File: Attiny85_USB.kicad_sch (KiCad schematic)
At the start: 0 parts

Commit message: Add full KiCad project with symbols and backups
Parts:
- added C1: 100n, Capacitor_SMD:C_1206_3216Metric_Pad1.33x1.80mm_HandSolder, symbol Device:C
- added D1, D2: 3V6, Diode_SMD:D_SOD-123, symbol Device:D_Zener
- added D3: LED, symbol Device:LED
- added J1, J2: Conn_01x04, symbol Connector_Generic:Conn_01x04
- added R1, R2: 68R, Resistor_SMD:R_0805_2012Metric_Pad1.20x1.40mm_HandSolder, symbol Device:R
- added R3: 330R, Resistor_SMD:R_0805_2012Metric_Pad1.20x1.40mm_HandSolder, symbol Device:R
- added R4: 1k5, Resistor_SMD:R_0805_2012Metric_Pad1.20x1.40mm_HandSolder, symbol Device:R
- added U1: ATtiny85-20M, Package_DFN_QFN:QFN-20-1EP_4x4mm_P0.5mm_EP2.6x2.6mm, symbol MCU_Microchip_ATtiny:ATtiny85-20M
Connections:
- new net: D2.1 (K), R2.2, R4.2
- new net: D1.1 (K), R1.2
- new net: J1.1 (Pin_1), U1.11 (AREF/PB0)
- new net: J1.2 (Pin_2), R3.1, U1.12 (PB1)
- new net: J1.3 (Pin_3), U1.14 (PB2)
- new net: J2.2 (Pin_2), R2.1, U1.2 (XTAL1/PB3)
- new net: D3.2 (A), R3.2
- new net: J2.3 (Pin_3), R1.1, U1.5 (XTAL2/PB4)
- new net: J2.1 (Pin_1), U1.1 (~{RESET}/PB5)
- new net +5V: C1.1, J1.4 (Pin_4), R4.1, U1.15 (VCC)
- new net GND: C1.2, D1.2 (A), D2.2 (A), D3.1 (K), J2.4 (Pin_4), U1.21 (GND), U1.8 (GND)

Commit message: added my symbol
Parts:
- added U2: ~, symbol my_symbol:PCB_USB_connector
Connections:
- net +5V: now also U2.1 (Vcc)
- net GND: now also U2.4 (GND)
- net at D2.1 (K), R2.2, R4.2: now also U2.2 (D+)
- net at D1.1 (K), R1.2: now also U2.3 (D-)
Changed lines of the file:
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@@
+	)
+	(junction
+		(at 156.21 57.15)
+		(diameter 0)
+		(color 0 0 0 0)
 	)
 	(junction
@@
 	)
 	(junction
+		(at 168.91 96.52)
+		(diameter 0)
+		(color 0 0 0 0)
+	)
+	(junction
 		(at 156.21 63.5)
 		(diameter 0)
@@
 	)
 	(junction
+		(at 156.21 33.02)
+		(diameter 0)
+		(color 0 0 0 0)
+	)
+	(junction
+		(at 168.91 67.31)
+		(diameter 0)
+		(color 0 0 0 0)
+	)
+	(junction
 		(at 119.38 62.23)
 		(diameter 0)
@@
 	(wire
 		(pts
+			(xy 182.88 96.52) (xy 168.91 96.52)
+		)
+		(stroke
+			(width 0)
+			(type default)
+		)
+	)
+	(wire
+		(pts
 			(xy 168.91 96.52) (xy 168.91 91.44)
 		)
@@
 	(wire
 		(pts
+			(xy 170.18 53.34) (xy 170.18 33.02)
+		)
+		(stroke
+			(width 0)
+			(type default)
+		)
+	)
+	(wire
+		(pts
 			(xy 120.65 62.23) (xy 119.38 62.23)
 		)
@@
 	(wire
 		(pts
+			(xy 182.88 60.96) (xy 168.91 60.96)
+		)
+		(stroke
+			(width 0)
+			(type default)
+		)
+	)
+	(wire
+		(pts
 			(xy 77.47 96.52) (xy 129.54 96.52)
 		)
@@
 	(wire
 		(pts
+			(xy 156.21 57.15) (xy 182.88 57.15)
+		)
+		(stroke
+			(width 0)
+			(type default)
+		)
+	)
+	(wire
+		(pts
 			(xy 111.76 57.15) (xy 92.71 57.15)
 		)
@@
 	(wire
 		(pts
+			(xy 182.88 53.34) (xy 170.18 53.34)
+		)
+		(stroke
+			(width 0)
+			(type default)
+		)
+	)
+	(wire
+		(pts
 			(xy 35.56 96.52) (xy 77.47 96.52)
 		)
@@
 	(wire
 		(pts
+			(xy 156.21 57.15) (xy 156.21 45.72)
+		)
+		(stroke
+			(width 0)
+			(type default)
+		)
+	)
+	(wire
+		(pts
 			(xy 35.56 58.42) (xy 35.56 33.02)
 		)
@@
 	(wire
 		(pts
-			(xy 156.21 63.5) (xy 156.21 45.72)
+			(xy 156.21 63.5) (xy 156.21 57.15)
 		)
 		(stroke
@@
 	(wire
 		(pts
+			(xy 182.88 64.77) (xy 182.88 96.52)
+		)
+		(stroke
+			(width 0)
+			(type default)
+		)
+	)
+	(wire
+		(pts
+			(xy 168.91 60.96) (xy 168.91 67.31)
+		)
+		(stroke
+			(width 0)
+			(type default)
+		)
+	)
+	(wire
+		(pts
 			(xy 156.21 91.44) (xy 156.21 96.52)
 		)
@@
 		(pts
 			(xy 121.92 67.31) (xy 121.92 85.09)
+		)
+		(stroke
+			(width 0)
+			(type default)
+		)
+	)
+	(wire
+		(pts
+			(xy 170.18 33.02) (xy 156.21 33.02)
 		)
 		(stroke
@@
 					(unit 1)
 				)
+			)
+		)
+	)
+	(symbol
+		(lib_id "my_symbol:PCB_USB_connector")
+		(at 195.58 57.15 0)
+		(unit 1)
+		(exclude_from_sim no)
+		(in_bom yes)
+		(on_board yes)
+		(dnp no)
+		(fields_autoplaced yes)
+		(property "Reference" "U2"
+			(at 195.58 57.15 0)
+			(effects
+				(font
+					(size 1.27 1.27)
+					(thickness 0.1588)
+				)
+				(hide yes)
+			)
+		)
+		(property "Value" "~"
+			(at 204.47 59.0549 0)
+			(effects
+				(font
+					(size 1.27 1.27)
+				)
+				(justify left)
+			)
+		)
+		(property "Footprint" ""
+			(at 195.58 57.15 0)
+			(effects
+				(font
+					(size 1.27 1.27)
+				)
+				(hide yes)
+			)
+		)
+		(property "Datasheet" ""
+			(at 195.58 57.15 0)
+			(effects
+				(font
+					(size 1.27 1.27)
+				)
+				(hide yes)
+			)
+		)
+		(property "Description" ""
+			(at 195.58 57.15 0)
+			(effects
+				(font
+					(size 1.27 1.27)
+				)
+				(hide yes)
+			)
+		)
+		(pin "3"
+		)
+		(pin "4"
+		)
+		(pin "1"
+		)
+		(pin "2"
+		)
+		(instances
+			(project ""
+				(path "/25dfa8f9-f095-4fc2-8dfc-eefd4e5bea23"
+					(reference "U2")
+					(unit 1)
+				)

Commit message: Correctoin of led et connectors feetprint
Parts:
- D3: footprint (none) -> LED_THT:LED_D3.0mm
- J1, J2: footprint (none) -> Connector_PinHeader_2.54mm:PinHeader_1x04_P2.54mm_Vertical
- U2: footprint (none) -> 1_my_LIB:my_footprint
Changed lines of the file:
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@@
 			)
 		)
-		(property "Footprint" ""
+		(property "Footprint" "1_my_LIB:my_footprint"
 			(at 195.58 57.15 0)
 			(effects
@@
 			)
 		)
-		(property "Footprint" ""
+		(property "Footprint" "Connector_PinHeader_2.54mm:PinHeader_1x04_P2.54mm_Vertical"
 			(at 111.76 39.37 0)
 			(effects
@@
 			)
 		)
-		(property "Footprint" ""
+		(property "Footprint" "LED_THT:LED_D3.0mm"
 			(at 143.51 87.63 0)
 			(effects
@@
 			)
 		)
-		(property "Footprint" ""
+		(property "Footprint" "Connector_PinHeader_2.54mm:PinHeader_1x04_P2.54mm_Vertical"
 			(at 119.38 90.17 0)
 			(effects

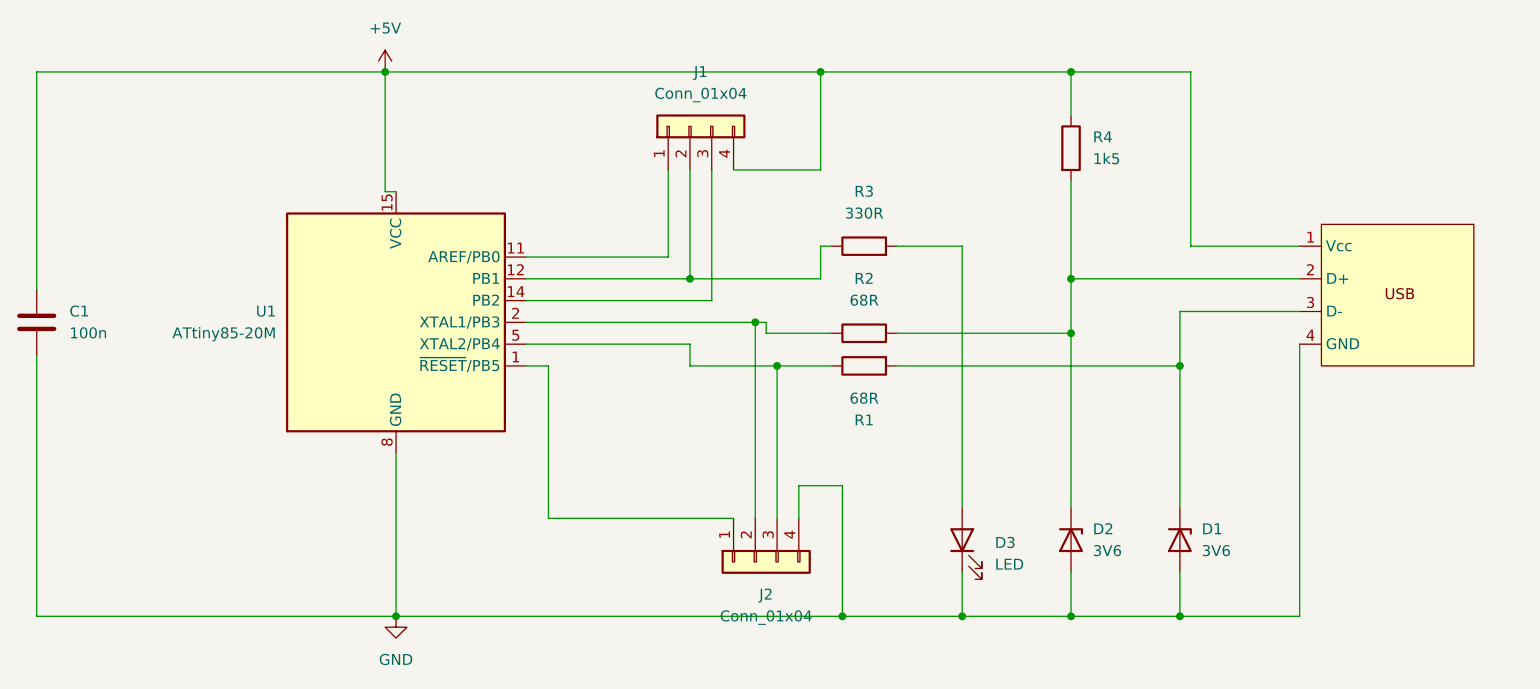
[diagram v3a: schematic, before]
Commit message: fixing some bugs on the printfoot of the ATtiny85
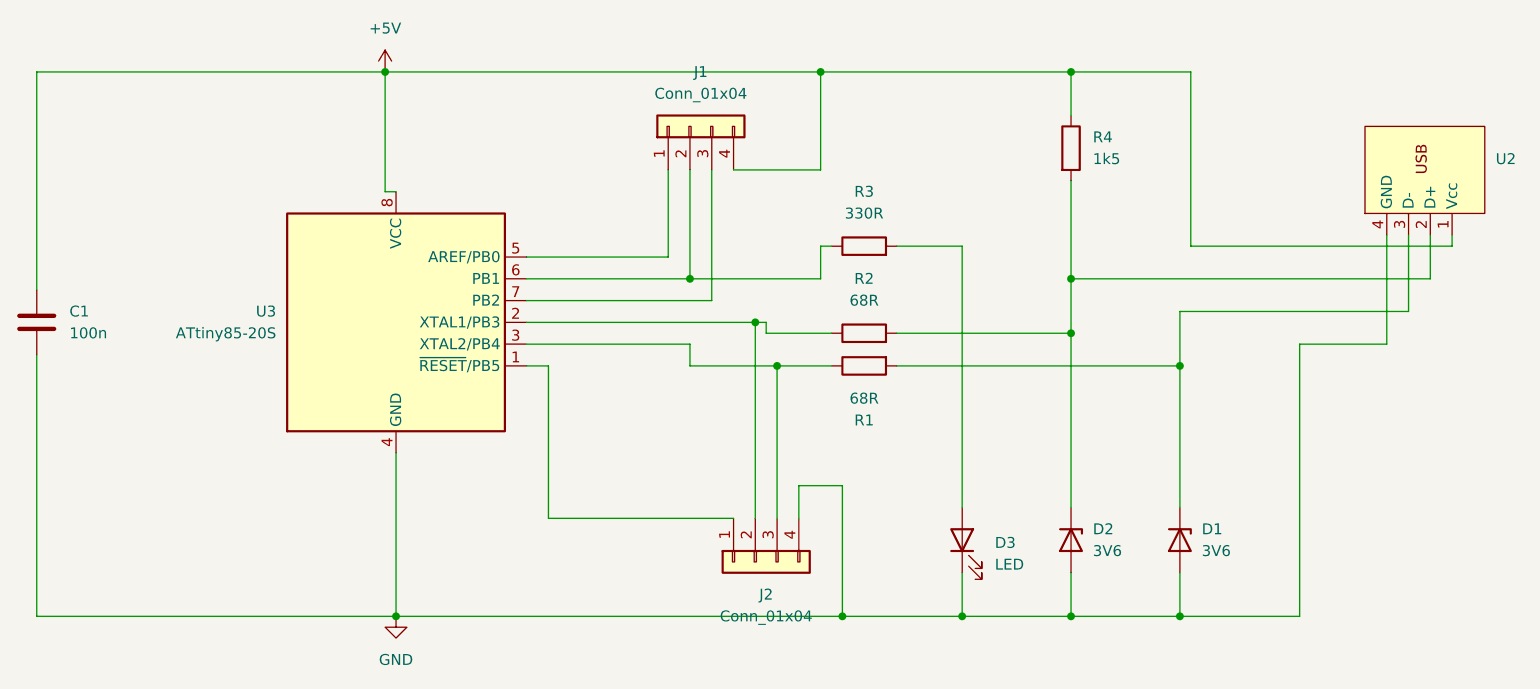
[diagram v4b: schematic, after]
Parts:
- removed U1: ATtiny85-20M, Package_DFN_QFN:QFN-20-1EP_4x4mm_P0.5mm_EP2.6x2.6mm, symbol MCU_Microchip_ATtiny:ATtiny85-20M
- removed U2: ~, 1_my_LIB:my_footprint, symbol my_symbol:PCB_USB_connector
- added U2: ~, 1_my_LIB:my_footprint, symbol New_Library:PCB_USB_CONECT
- added U3: ATtiny85-20S, Package_SO:SOIC-8_5.3x5.3mm_P1.27mm, symbol MCU_Microchip_ATtiny:ATtiny85-20S
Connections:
- net +5V: now also U2.1 (Vcc), U3.8 (VCC)
- net GND: now also U2.4 (GND), U3.4 (GND)
- net at D2.1 (K), R2.2, R4.2: now also U2.2 (D+)
- net at D1.1 (K), R1.2: now also U2.3 (D-)
- net at J1.1 (Pin_1): now also U3.5 (AREF/PB0)
- net at J1.2 (Pin_2), R3.1: now also U3.6 (PB1)
- net at J1.3 (Pin_3): now also U3.7 (PB2)
- net at J2.2 (Pin_2), R2.1: now also U3.2 (XTAL1/PB3)
- net at J2.3 (Pin_3), R1.1: now also U3.3 (XTAL2/PB4)
- net at J2.1 (Pin_1): now also U3.1 (~{RESET}/PB5)
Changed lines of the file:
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@@
 	(wire
 		(pts
-			(xy 182.88 60.96) (xy 168.91 60.96)
+			(xy 195.58 52.07) (xy 195.58 60.96)
+		)
+		(stroke
+			(width 0)
+			(type default)
+		)
+	)
+	(wire
+		(pts
+			(xy 168.91 60.96) (xy 195.58 60.96)
 		)
 		(stroke
@@
 	(wire
 		(pts
+			(xy 200.66 52.07) (xy 200.66 53.34)
+		)
+		(stroke
+			(width 0)
+			(type default)
+		)
+	)
+	(wire
+		(pts
 			(xy 35.56 33.02) (xy 76.2 33.02)
 		)
@@
 	(wire
 		(pts
-			(xy 156.21 57.15) (xy 182.88 57.15)
+			(xy 156.21 57.15) (xy 198.12 57.15)
 		)
 		(stroke
@@
 	(wire
 		(pts
-			(xy 182.88 53.34) (xy 170.18 53.34)
+			(xy 170.18 53.34) (xy 200.66 53.34)
 		)
 		(stroke
@@
 	(wire
 		(pts
+			(xy 198.12 52.07) (xy 198.12 57.15)
+		)
+		(stroke
+			(width 0)
+			(type default)
+		)
+	)
+	(wire
+		(pts
 			(xy 127 57.15) (xy 111.76 57.15)
 		)
@@
 	(wire
 		(pts
+			(xy 193.04 52.07) (xy 193.04 64.77)
+		)
+		(stroke
+			(width 0)
+			(type default)
+		)
+	)
+	(wire
+		(pts
 			(xy 121.92 67.31) (xy 121.92 85.09)
 		)
@@
 		(pts
 			(xy 143.51 96.52) (xy 156.21 96.52)
+		)
+		(stroke
+			(width 0)
+			(type default)
+		)
+	)
+	(wire
+		(pts
+			(xy 193.04 64.77) (xy 182.88 64.77)
 		)
 		(stroke
@@
 	)
 	(symbol
-		(lib_id "my_symbol:PCB_USB_connector")
-		(at 195.58 57.15 0)
+		(lib_id "New_Library:PCB_USB_CONECT")
+		(at 196.85 52.07 90)
 		(unit 1)
 		(exclude_from_sim no)
@@
 		(fields_autoplaced yes)
 		(property "Reference" "U2"
-			(at 195.58 57.15 0)
-			(effects
-				(font
-					(size 1.27 1.27)
-					(thickness 0.1588)
-				)
-				(hide yes)
+			(at 205.74 43.1799 90)
+			(effects
+				(font
+					(size 1.27 1.27)
+				)
+				(justify right)
 			)
 		)
 		(property "Value" "~"
-			(at 204.47 59.0549 0)
-			(effects
-				(font
-					(size 1.27 1.27)
-				)
-				(justify left)
+			(at 205.74 45.7199 90)
+			(effects
+				(font
+					(size 1.27 1.27)
+				)
+				(justify right)
 			)
 		)
 		(property "Footprint" "1_my_LIB:my_footprint"
-			(at 195.58 57.15 0)
+			(at 196.85 52.07 0)
 			(effects
 				(font
@@
 		)
 		(property "Datasheet" ""
-			(at 195.58 57.15 0)
+			(at 196.85 52.07 0)
 			(effects
 				(font
@@
 		)
 		(property "Description" ""
-			(at 195.58 57.15 0)
-			(effects
-				(font
-					(size 1.27 1.27)
-				)
-				(hide yes)
-			)
+			(at 196.85 52.07 0)
+			(effects
+				(font
+					(size 1.27 1.27)
+				)
+				(hide yes)
+			)
+		)
+		(pin "2"
+		)
+		(pin "1"
+		)
+		(pin "4"
 		)
 		(pin "3"
-		)
-		(pin "4"
-		)
-		(pin "1"
-		)
-		(pin "2"
 		)
 		(instances
@@
 				(path "/25dfa8f9-f095-4fc2-8dfc-eefd4e5bea23"
 					(reference "U2")
+					(unit 1)
+				)
+			)
+		)
+	)
+	(symbol
+		(lib_id "MCU_Microchip_ATtiny:ATtiny85-20S")
+		(at 77.47 62.23 0)
+		(unit 1)
+		(exclude_from_sim no)
+		(in_bom yes)
+		(on_board yes)
+		(dnp no)
+		(fields_autoplaced yes)
+		(property "Reference" "U3"
+			(at 63.5 60.9599 0)
+			(effects
+				(font
+					(size 1.27 1.27)
+				)
+				(justify right)
+			)
+		)
+		(property "Value" "ATtiny85-20S"
+			(at 63.5 63.4999 0)
+			(effects
+				(font
+					(size 1.27 1.27)
+				)
+				(justify right)
+			)
+		)
+		(property "Footprint" "Package_SO:SOIC-8_5.3x5.3mm_P1.27mm"
+			(at 77.47 62.23 0)
+			(effects
+				(font
+					(size 1.27 1.27)
+					(italic yes)
+				)
+				(hide yes)
+			)
+		)
+		(property "Datasheet" "http://ww1.microchip.com/downloads/en/DeviceDoc/atmel-2586-avr-8-bit-microcontroller-attiny25-attiny45-attiny85_datasheet.pdf"
+			(at 77.47 62.23 0)
+			(effects
+				(font
+					(size 1.27 1.27)
+				)
+				(hide yes)
+			)
+		)
+		(property "Description" "20MHz, 8kB Flash, 512B SRAM, 512B EEPROM, debugWIRE, SOIC-8"
+			(at 77.47 62.23 0)
+			(effects
+				(font
+					(size 1.27 1.27)
+				)
+				(hide yes)
+			)
+		)
+		(pin "5"
+		)
+		(pin "4"
+		)
+		(pin "2"
+		)
+		(pin "6"
+		)
+		(pin "3"
+		)
+		(pin "8"
+		)
+		(pin "7"
+		)
+		(pin "1"
+		)
+		(instances
+			(project ""
+				(path "/25dfa8f9-f095-4fc2-8dfc-eefd4e5bea23"
+					(reference "U3")
 					(unit 1)
 				)
@@
 					(unit 1)
 				)
-			)
-		)
-	)
-	(symbol
-		(lib_id "MCU_Microchip_ATtiny:ATtiny85-20M")
-		(at 77.47 62.23 0)
-		(unit 1)
-		(exclude_from_sim no)
-		(in_bom yes)
-		(on_board yes)
-		(dnp no)
-		(fields_autoplaced yes)
-		(property "Reference" "U1"
-			(at 63.5 60.9599 0)
-			(effects
-				(font
-					(size 1.27 1.27)
-				)
-				(justify right)
-			)
-		)
-		(property "Value" "ATtiny85-20M"
-			(at 63.5 63.4999 0)
-			(effects
-				(font
-					(size 1.27 1.27)
-				)
-				(justify right)
-			)
-		)
-		(property "Footprint" "Package_DFN_QFN:QFN-20-1EP_4x4mm_P0.5mm_EP2.6x2.6mm"
-			(at 77.47 62.23 0)
-			(effects
-				(font
-					(size 1.27 1.27)
-					(italic yes)
-				)
-				(hide yes)
-			)
-		)
-		(property "Datasheet" "http://ww1.microchip.com/downloads/en/DeviceDoc/atmel-2586-avr-8-bit-microcontroller-attiny25-attiny45-attiny85_datasheet.pdf"
-			(at 77.47 62.23 0)
-			(effects
-				(font
-					(size 1.27 1.27)
-				)
-				(hide yes)
-			)
-		)
-		(property "Description" "20MHz, 8kB Flash, 512B SRAM, 512B EEPROM, debugWIRE, QFN-20"
-			(at 77.47 62.23 0)
-			(effects
-				(font
-					(size 1.27 1.27)
-				)
-				(hide yes)
-			)
-		)
-		(pin "18"
-		)
-		(pin "20"
-		)
-		(pin "13"
-		)
-		(pin "11"
-		)
-		(pin "14"
-		)
-		(pin "17"
-		)
-		(pin "19"
-		)
-		(pin "1"
-		)
-		(pin "3"
-		)
-		(pin "9"
-		)
-		(pin "15"
-		)
-		(pin "10"
-		)
-		(pin "6"
-		)
-		(pin "7"
-		)
-		(pin "4"
-		)
-		(pin "16"
-		)
-		(pin "21"
-		)
-		(pin "8"
-		)
-		(pin "12"
-		)
-		(pin "2"
-		)
-		(pin "5"
-		)
-		(instances
-			(project ""
-				(path "/25dfa8f9-f095-4fc2-8dfc-eefd4e5bea23"
-					(reference "U1")
-					(unit 1)
-				)
